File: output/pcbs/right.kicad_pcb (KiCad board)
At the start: 2 copper layers, 139.8 x 121.8 mm, 64 parts

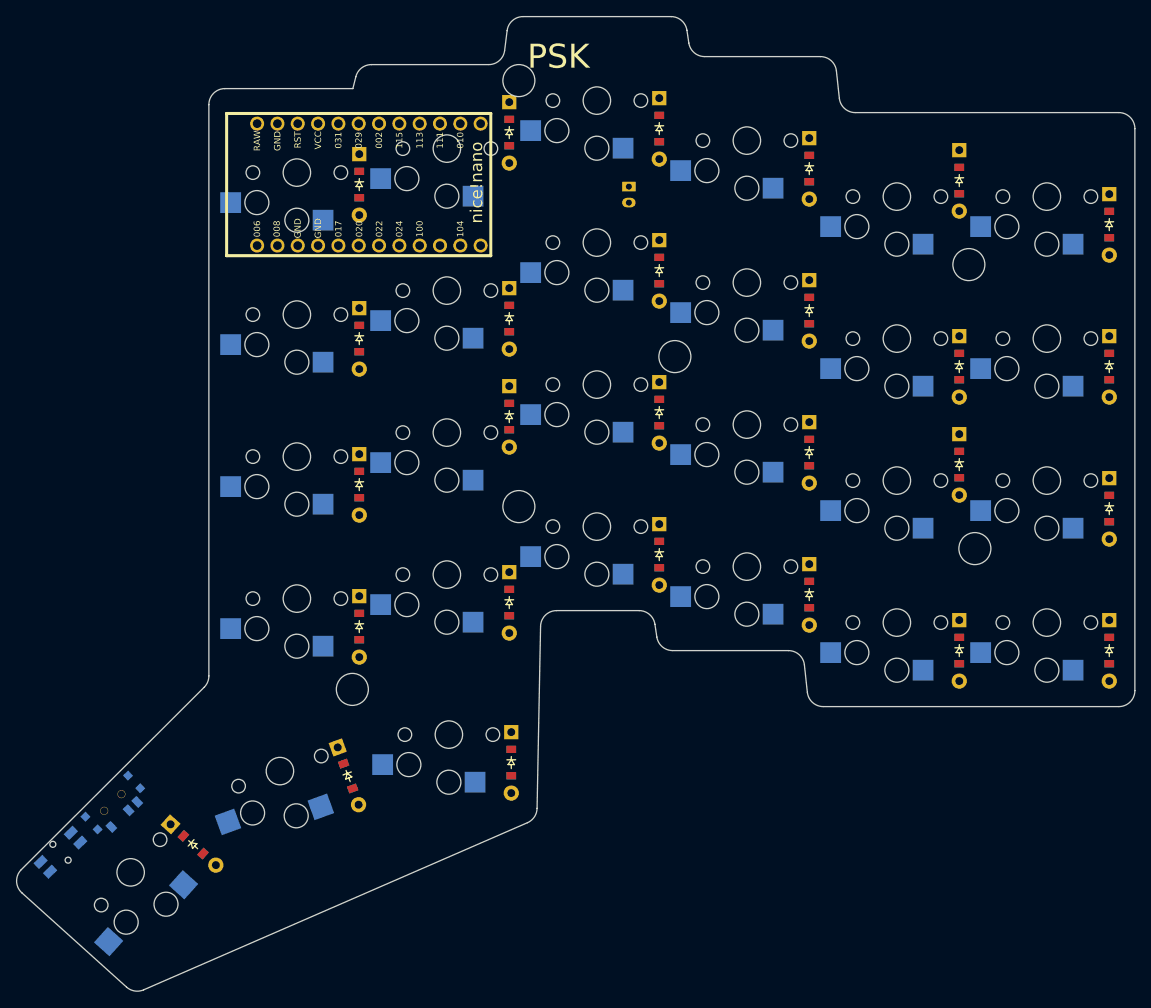
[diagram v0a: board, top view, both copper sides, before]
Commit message: clean slate, regenerated without trash routes
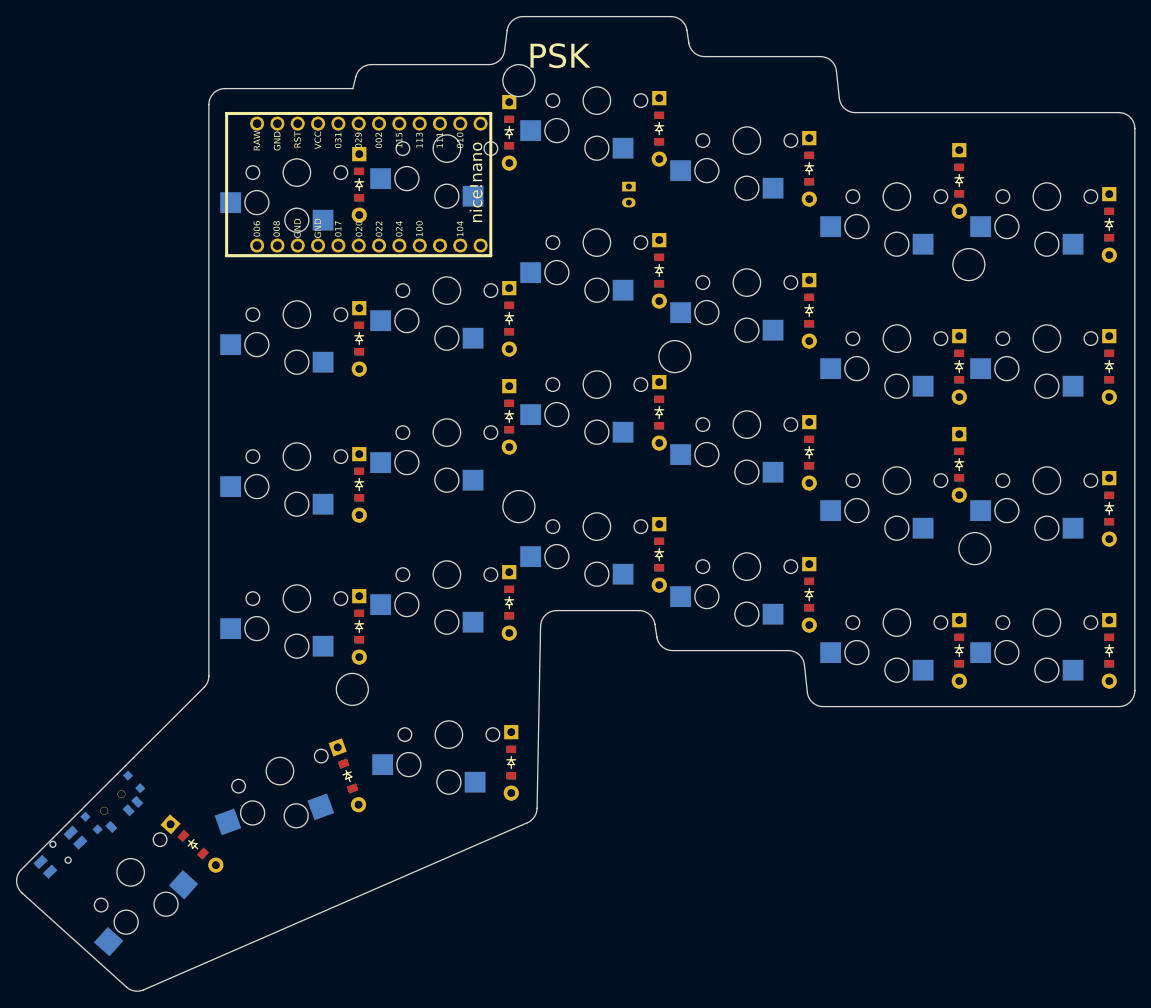
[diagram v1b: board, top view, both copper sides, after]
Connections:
- D18 pad 1: (no net) -> P031
- D19 pad 1: (no net) -> P031
- D20 pad 1: (no net) -> P031
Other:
- outline, holes or cut-outs redrawn
- net class Default added: clearance 0.2, trace_width 0.25, via_dia 0.8, via_drill 0.4

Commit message: routed left, removed top left mounting hole from left and right and yaml
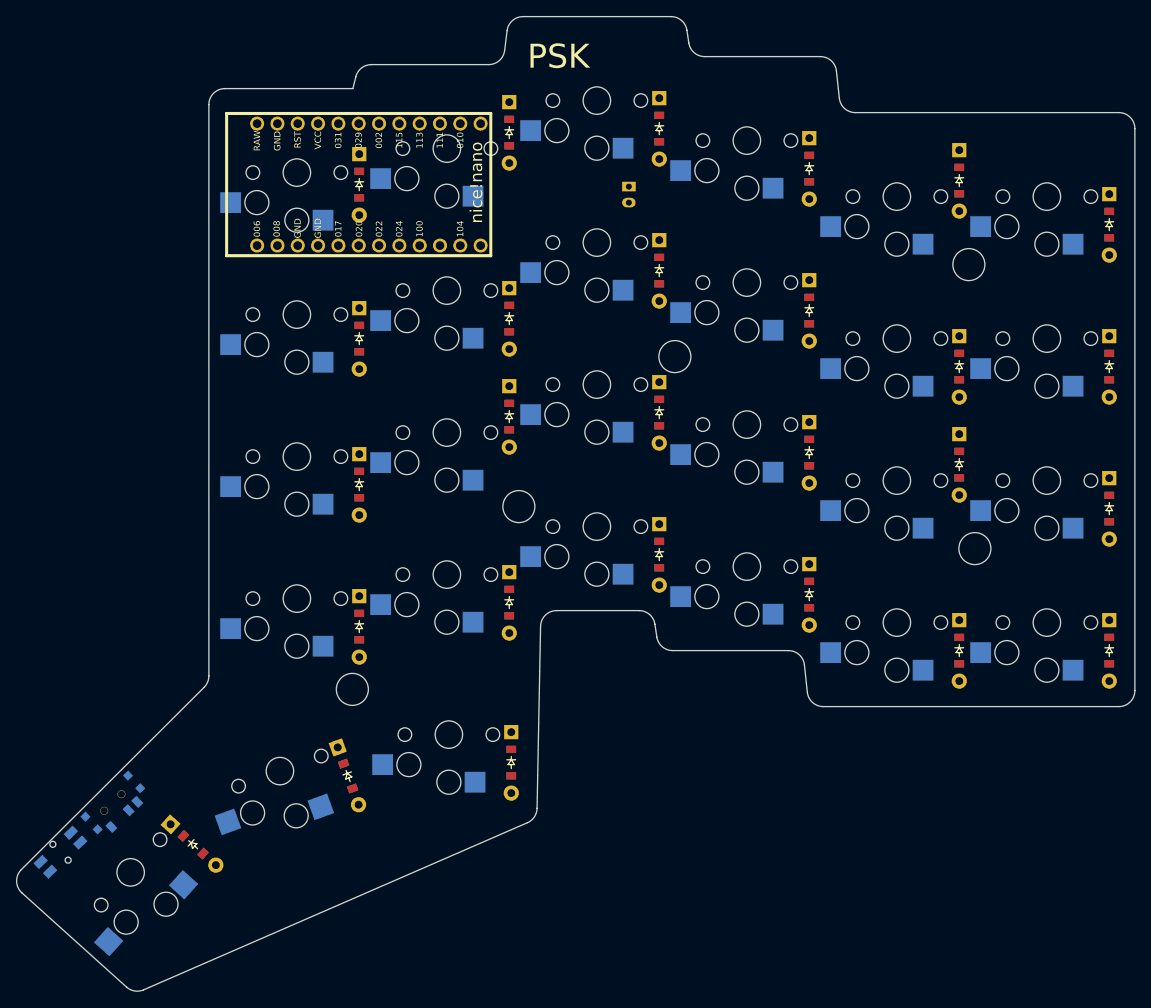
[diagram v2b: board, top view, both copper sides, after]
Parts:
- removed the ? at (321.5, 82.2)
- removed the ? at (300.7, 158.3)
- added ?: , HOLE_M2_TH, F.Cu at (300.7, 158.3)
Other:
- outline, holes or cut-outs redrawn
- net class Default removed
